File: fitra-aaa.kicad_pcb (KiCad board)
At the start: 4 copper layers, 38.5 x 14.2 mm, 23 parts, among them J1 SM03B-SRSS-TB, M1 *, U2 LSM6DSV, U3 NPM2100-QEAA-R7

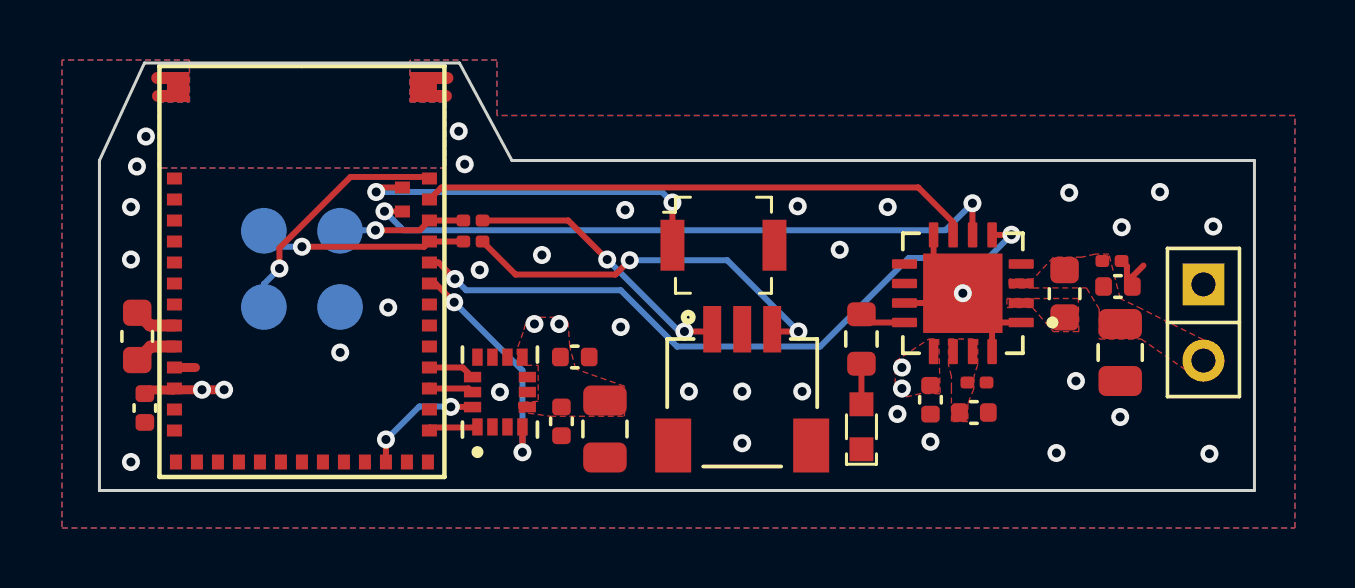
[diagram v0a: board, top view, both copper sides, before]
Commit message: Update board for AN54LV module
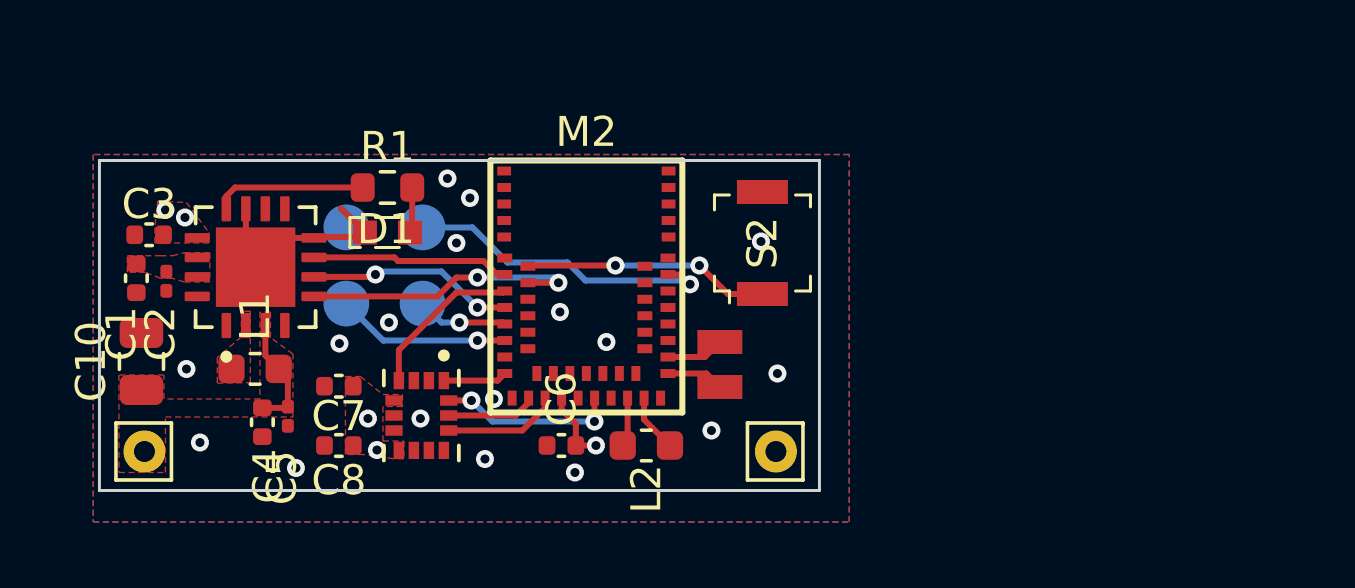
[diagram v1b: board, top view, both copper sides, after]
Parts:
- removed BAT_thru2: ~, local_lib:VBAT_thru
- removed C9: 100uF, Capacitor_SMD:C_0805_2012Metric
- removed M1: *, AN54LQ-15_PCBLIB_250212:AN54LQ-15
- removed R2, R3: 100Ω, Resistor_SMD:R_0201_0603Metric
- added J2: Conn_01x01_Pin, Connector_Pin:Pin_D0.7mm_L6.5mm_W1.8mm_FlatFork, F.Cu at (106.0, 68.2)
- added M2: AN54LV-15, AN54LV-15-250919:AN54LV-15, F.Cu at (99.7, 58.5)
- added Y2: CM8V-T1A-32.768KHZ-6PF-20PPM-TA-QC, se_CM8V-T1A-32.768KHZ-6PF-20PPM-TA-QC:XTAL_CM8V-T1A-32.768KHZ-6PF-20PPM-TA-QC, F.Cu at (104.2, 65.3)
- J1: value SM03B-SRSS-TB -> Conn_01x01_Pin; footprint sm03b_lib:JST_SM03B-SRSS-TB_LF__SN_ -> Connector_Pin:Pin_D0.7mm_L6.5mm_W1.8mm_FlatFork
- moved C10 32.6 mm to (84.9, 65.2), turned to 90 degrees
- moved C4 28.9 mm to (88.9, 67.2), turned to -90 degrees
- moved C1 28.3 mm to (84.7, 62.4), turned to -90 degrees
- moved C5 28.0 mm to (89.8, 67.0), turned to -90 degrees
- moved C2 27.2 mm to (85.7, 62.5), turned to -90 degrees
- moved L1 27.1 mm to (88.7, 65.4), turned to 180 degrees
- moved C3 26.6 mm to (85.2, 61.0), turned to 180 degrees
- moved U3 23.6 mm to (88.7, 62.1), turned to 90 degrees
- moved J1 20.3 mm to (85.0, 68.2)
- moved L2 17.4 mm to (101.7, 68.0), turned to 180 degrees
- moved D1 17.1 mm to (93.1, 60.9), turned to 0 degrees
- moved R1 16.6 mm to (93.1, 59.4), turned to 180 degrees
- moved C6 13.9 mm to (98.9, 68.0), turned to 180 degrees
- moved C8 8.40 mm to (91.5, 68.0), turned to 180 degrees
- moved C7 7.51 mm to (91.5, 66.0), turned to 180 degrees
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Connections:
- J1 pad 1: Net-(J1-Pad1) -> +BATT
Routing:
- net SDA: track 21.9 -> 6.97 mm
- net GPIO0: track 22.8 -> 9.50 mm
- net Net-(J1-Pad3): track 13.0 -> 0.00 mm, vias 2 -> 0
- net SCL: track 18.5 -> 6.60 mm
- net Net-(J1-Pad1): track 9.19 -> 0.00 mm, vias 2 -> 0
- net GND: track 12.9 -> 7.33 mm, vias 32 -> 17
- net SW0: track 12.4 -> 8.22 mm
- net +BATT: track 0.00 -> 4.13 mm
- net SWDIO: track 6.94 -> 3.02 mm
- net LED1: track 1.55 -> 5.09 mm
- net INT1: track 7.85 -> 5.36 mm, vias 2 -> 0
- net RESET: track 8.18 -> 10.6 mm
- net CS: track 1.56 -> 3.85 mm
- net SDI: track 3.99 -> 5.93 mm
- net XL1: track 0.00 -> 1.94 mm
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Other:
- board size 38.5 x 14.2 mm -> 24 x 11 mm
